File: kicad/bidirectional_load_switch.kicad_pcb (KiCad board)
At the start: 2 copper layers, 10 parts, among them U1 SISS94DN-T1-GE3, U2 RTBS60M, U3 UCC23313DWYR, U4 DMN65D8L-7

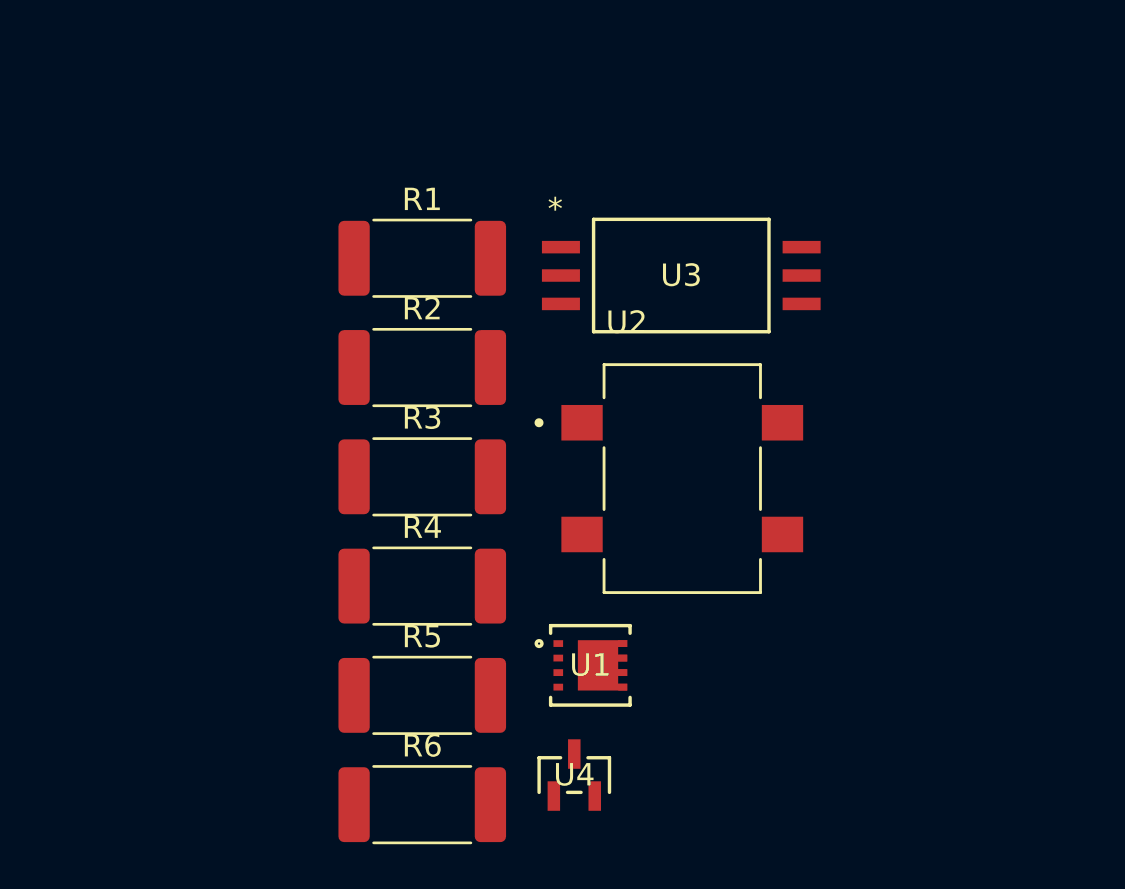
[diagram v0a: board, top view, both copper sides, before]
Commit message: implementing switch design
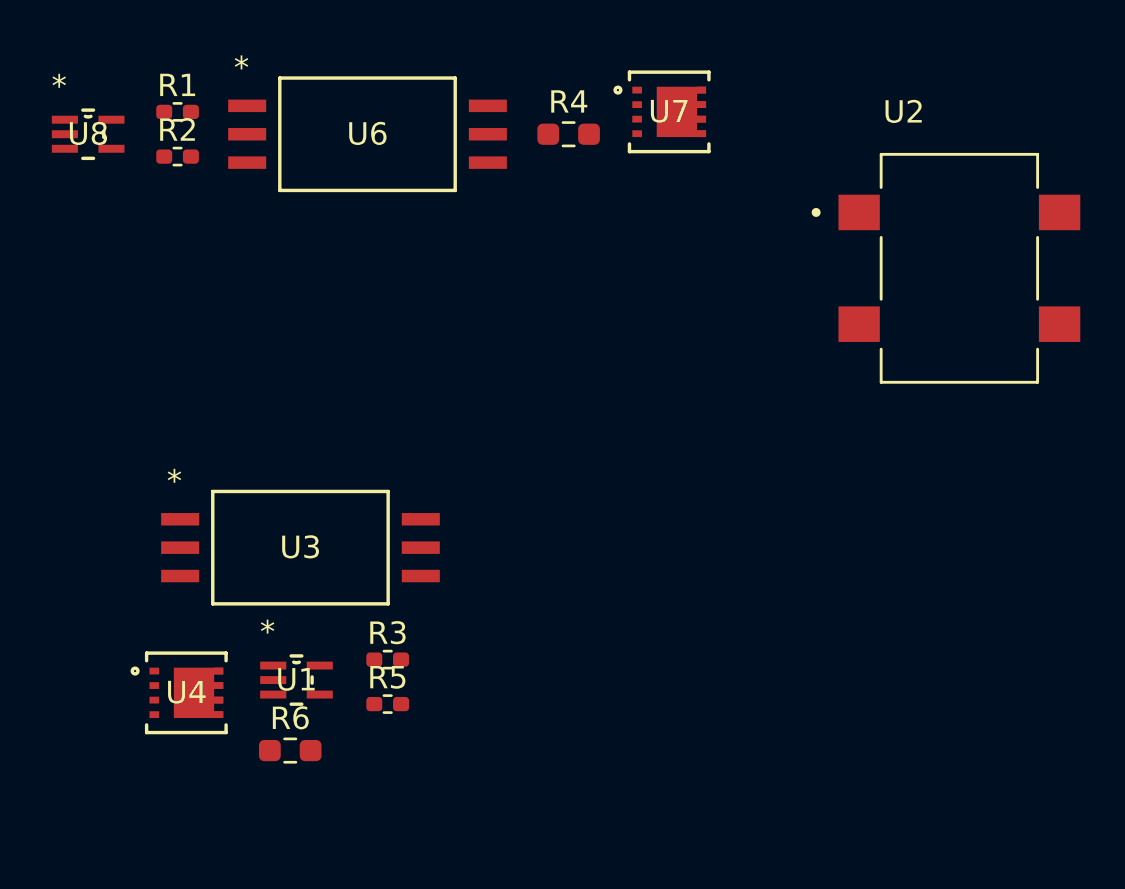
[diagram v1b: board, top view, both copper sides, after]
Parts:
- added U6: UCC23313DWYR, Gate Driver:SOIC6_DWY_TEX, F.Cu at (37.5, 28.0)
- added U7: SISS94DN-T1-GE3, Switching Mosfet:MOSFET_3DN-T1-GE3_VIS, F.Cu at (51.0, 27.0)
- added U8: SN74LVC1G17DCKR, Buffer:DCK5, F.Cu at (25.0, 28.0)
- R1, R2, R3, R5: value R_US -> 50; footprint Resistor_SMD:R_2512_6332Metric_Pad1.40x3.35mm_HandSolder -> Resistor_SMD:R_0402_1005Metric_Pad0.72x0.64mm_HandSolder
- R4, R6: value R_US -> 10; footprint Resistor_SMD:R_2512_6332Metric_Pad1.40x3.35mm_HandSolder -> Resistor_SMD:R_0603_1608Metric_Pad0.98x0.95mm_HandSolder
- U1: value SISS94DN-T1-GE3 -> SN74LVC1G17DCKR; footprint Big Mosfet:MOSFET_3DN-T1-GE3_VIS -> Buffer:DCK5
- U4: value DMN65D8L-7 -> SISS94DN-T1-GE3; footprint Small Mosfet:SOT-23_2P9X1P3_DIO -> Switching Mosfet:MOSFET_3DN-T1-GE3_VIS
- moved R4 21.3 mm to (46.5, 28.0)
- moved U3 20.9 mm to (34.5, 46.5)
- moved U4 17.7 mm to (29.4, 53.0)
- moved U2 15.6 mm to (64.0, 34.0)
- moved R2 14.5 mm to (29.0, 29.0)
- moved U1 13.2 mm to (34.3, 52.4)
- moved R1 12.8 mm to (29.0, 27.0)
- moved R3 8.33 mm to (38.4, 51.5)
- moved R6 6.38 mm to (34.0, 55.6)
- moved R5 1.60 mm to (38.4, 53.5)
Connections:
- R1 pad 1: Net-(U3-VOUT) -> Net-(U8-Y)
- R1 pad 2: Net-(U1-G) -> Net-(U6-ANODE)
- R2 pad 1: GNDPWR -> GND
- R2 pad 2: Net-(U1-G) -> Net-(U6-CATHODE)
- R3 pad 1: Net-(R3-Pad1) -> Net-(U1-Y)
- R3 pad 2: Net-(R3-Pad2) -> Net-(U3-ANODE)
- R4 pad 1: Net-(U3-CATHODE) -> Net-(U6-VOUT)
- R4 pad 2: Net-(U4-D) -> Net-(U7-G)
- R5 pad 1: +3V3 -> GND
- R5 pad 2: Net-(U3-ANODE) -> Net-(U3-CATHODE)
- R6 pad 1: unconnected-(R6-Pad1) -> Net-(U3-VOUT)
- U1 pad 1: GNDPWR -> unconnected-(U1-NC-Pad1)
- U1 pad 2: GNDPWR -> /Switching Channel 1/EN
- U1 pad 3: GNDPWR -> GND
- U1 pad 4: Net-(U1-G) -> Net-(U1-Y)
- U1 pad 5: Net-(R3-Pad2) -> +3V3
- U2 pad 1: Net-(R3-Pad1) -> VS
- U2 pad 3: unconnected-(U2-Pad3) -> Earth
- U2 pad 4: unconnected-(U2-Pad4) -> AC
- U3 pad 6: +15V -> +20V
- U4 pad 1: Net-(U4-G) -> GNDPWR
- U4 pad 2: Net-(U4-D) -> GNDPWR
- U4 pad 3: GNDD -> GNDPWR

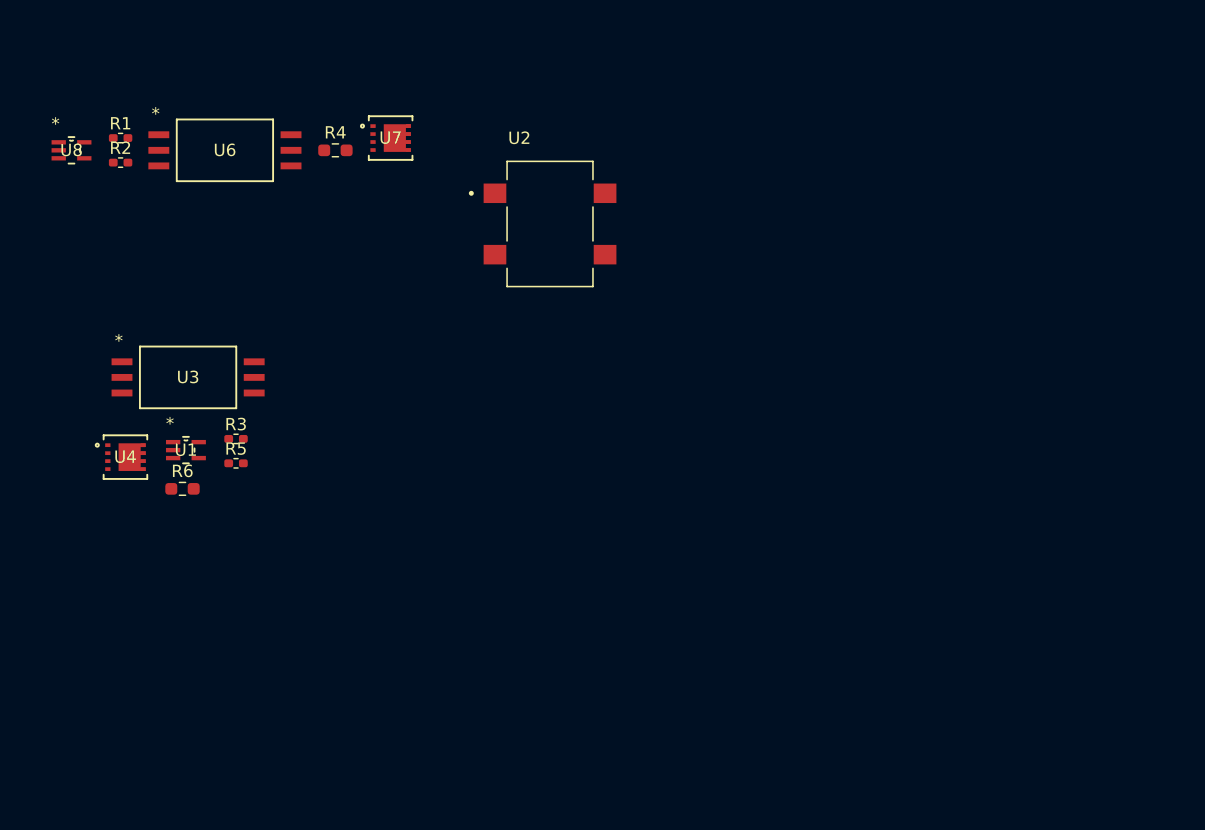
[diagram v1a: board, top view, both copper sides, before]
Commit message: updated switch topology
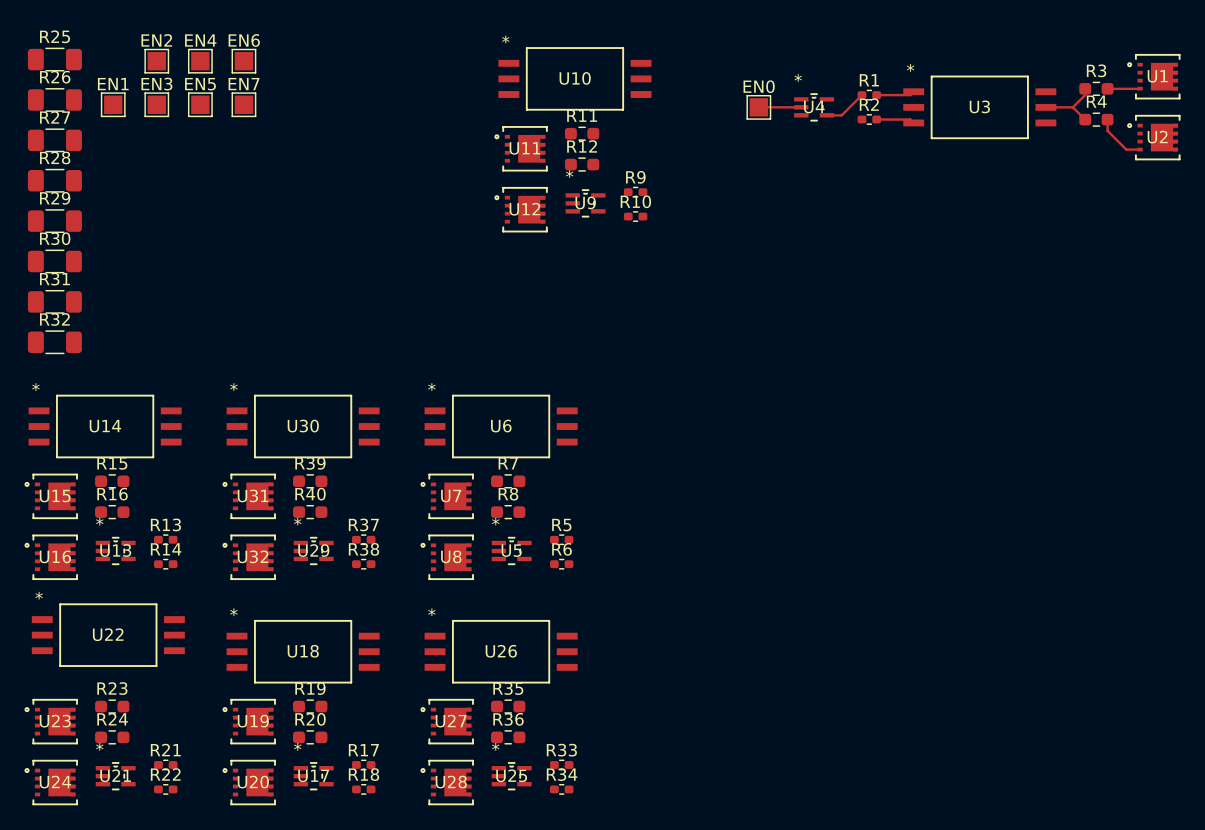
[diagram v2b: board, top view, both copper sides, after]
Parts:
- added EN0: TestPoint, TestPoint:TestPoint_Pad_1.5x1.5mm, F.Cu at (81.0, 24.5)
- added EN1: TestPoint, TestPoint:TestPoint_Pad_1.5x1.5mm, F.Cu at (28.4, 24.3)
- added EN2: TestPoint, TestPoint:TestPoint_Pad_1.5x1.5mm, F.Cu at (31.9, 20.7)
- added EN3: TestPoint, TestPoint:TestPoint_Pad_1.5x1.5mm, F.Cu at (31.9, 24.3)
- added EN4: TestPoint, TestPoint:TestPoint_Pad_1.5x1.5mm, F.Cu at (35.5, 20.7)
- added EN5: TestPoint, TestPoint:TestPoint_Pad_1.5x1.5mm, F.Cu at (35.5, 24.3)
- added EN6: TestPoint, TestPoint:TestPoint_Pad_1.5x1.5mm, F.Cu at (39.0, 20.7)
- added EN7: TestPoint, TestPoint:TestPoint_Pad_1.5x1.5mm, F.Cu at (39.0, 24.3)
- added R10: 50, Resistor_SMD:R_0402_1005Metric_Pad0.72x0.64mm_HandSolder, F.Cu at (71.0, 33.4)
- added R11: 10, Resistor_SMD:R_0603_1608Metric_Pad0.98x0.95mm_HandSolder, F.Cu at (66.6, 26.6)
- added R12: 10, Resistor_SMD:R_0603_1608Metric_Pad0.98x0.95mm_HandSolder, F.Cu at (66.6, 29.2)
- added R13: 50, Resistor_SMD:R_0402_1005Metric_Pad0.72x0.64mm_HandSolder, F.Cu at (32.7, 59.7)
- added R14: 50, Resistor_SMD:R_0402_1005Metric_Pad0.72x0.64mm_HandSolder, F.Cu at (32.7, 61.7)
- added R15: 10, Resistor_SMD:R_0603_1608Metric_Pad0.98x0.95mm_HandSolder, F.Cu at (28.3, 55.0)
- added R16: 10, Resistor_SMD:R_0603_1608Metric_Pad0.98x0.95mm_HandSolder, F.Cu at (28.3, 57.5)
- added R17: 50, Resistor_SMD:R_0402_1005Metric_Pad0.72x0.64mm_HandSolder, F.Cu at (48.8, 78.1)
- added R18: 50, Resistor_SMD:R_0402_1005Metric_Pad0.72x0.64mm_HandSolder, F.Cu at (48.8, 80.1)
- added R19: 10, Resistor_SMD:R_0603_1608Metric_Pad0.98x0.95mm_HandSolder, F.Cu at (44.4, 73.3)
- added R20: 10, Resistor_SMD:R_0603_1608Metric_Pad0.98x0.95mm_HandSolder, F.Cu at (44.4, 75.8)
- added R21: 50, Resistor_SMD:R_0402_1005Metric_Pad0.72x0.64mm_HandSolder, F.Cu at (32.7, 78.1)
- added R22: 50, Resistor_SMD:R_0402_1005Metric_Pad0.72x0.64mm_HandSolder, F.Cu at (32.7, 80.1)
- added R23: 10, Resistor_SMD:R_0603_1608Metric_Pad0.98x0.95mm_HandSolder, F.Cu at (28.3, 73.3)
- added R24: 10, Resistor_SMD:R_0603_1608Metric_Pad0.98x0.95mm_HandSolder, F.Cu at (28.3, 75.8)
- added R25: R_US, Resistor_SMD:R_1206_3216Metric_Pad1.30x1.75mm_HandSolder, F.Cu at (23.6, 20.6)
- added R26: R_US, Resistor_SMD:R_1206_3216Metric_Pad1.30x1.75mm_HandSolder, F.Cu at (23.6, 23.9)
- added R27: R_US, Resistor_SMD:R_1206_3216Metric_Pad1.30x1.75mm_HandSolder, F.Cu at (23.6, 27.2)
- added R28: R_US, Resistor_SMD:R_1206_3216Metric_Pad1.30x1.75mm_HandSolder, F.Cu at (23.6, 30.5)
- added R29: R_US, Resistor_SMD:R_1206_3216Metric_Pad1.30x1.75mm_HandSolder, F.Cu at (23.6, 33.8)
- added R30: R_US, Resistor_SMD:R_1206_3216Metric_Pad1.30x1.75mm_HandSolder, F.Cu at (23.6, 37.1)
- added R31: R_US, Resistor_SMD:R_1206_3216Metric_Pad1.30x1.75mm_HandSolder, F.Cu at (23.6, 40.3)
- added R32: R_US, Resistor_SMD:R_1206_3216Metric_Pad1.30x1.75mm_HandSolder, F.Cu at (23.6, 43.6)
- added R33: 50, Resistor_SMD:R_0402_1005Metric_Pad0.72x0.64mm_HandSolder, F.Cu at (64.9, 78.1)
- added R34: 50, Resistor_SMD:R_0402_1005Metric_Pad0.72x0.64mm_HandSolder, F.Cu at (64.9, 80.1)
- added R35: 10, Resistor_SMD:R_0603_1608Metric_Pad0.98x0.95mm_HandSolder, F.Cu at (60.6, 73.3)
- added R36: 10, Resistor_SMD:R_0603_1608Metric_Pad0.98x0.95mm_HandSolder, F.Cu at (60.6, 75.8)
- added R37: 50, Resistor_SMD:R_0402_1005Metric_Pad0.72x0.64mm_HandSolder, F.Cu at (48.8, 59.7)
- added R38: 50, Resistor_SMD:R_0402_1005Metric_Pad0.72x0.64mm_HandSolder, F.Cu at (48.8, 61.7)
- added R39: 10, Resistor_SMD:R_0603_1608Metric_Pad0.98x0.95mm_HandSolder, F.Cu at (44.4, 55.0)
- added R40: 10, Resistor_SMD:R_0603_1608Metric_Pad0.98x0.95mm_HandSolder, F.Cu at (44.4, 57.5)
- added R7: 10, Resistor_SMD:R_0603_1608Metric_Pad0.98x0.95mm_HandSolder, F.Cu at (60.6, 55.0)
- added R8: 10, Resistor_SMD:R_0603_1608Metric_Pad0.98x0.95mm_HandSolder, F.Cu at (60.6, 57.5)
- added R9: 50, Resistor_SMD:R_0402_1005Metric_Pad0.72x0.64mm_HandSolder, F.Cu at (71.0, 31.4)
- added U10: UCC23313DWYR, Gate Driver:SOIC6_DWY_TEX, F.Cu at (66.0, 22.2)
- added U11: SISS94DN-T1-GE3, Switching Mosfet:MOSFET_3DN-T1-GE3_VIS, F.Cu at (62.0, 27.9)
- added U12: SISS94DN-T1-GE3, Switching Mosfet:MOSFET_3DN-T1-GE3_VIS, F.Cu at (62.0, 32.8)
- added U13: SN74LVC1G17DCKR, Buffer:DCK5, F.Cu at (28.6, 60.6)
- added U14: UCC23313DWYR, Gate Driver:SOIC6_DWY_TEX, F.Cu at (27.7, 50.5)
- added U15: SISS94DN-T1-GE3, Switching Mosfet:MOSFET_3DN-T1-GE3_VIS, F.Cu at (23.7, 56.2)
- added U16: SISS94DN-T1-GE3, Switching Mosfet:MOSFET_3DN-T1-GE3_VIS, F.Cu at (23.7, 61.2)
- added U17: SN74LVC1G17DCKR, Buffer:DCK5, F.Cu at (44.7, 79.0)
- added U18: UCC23313DWYR, Gate Driver:SOIC6_DWY_TEX, F.Cu at (43.9, 68.8)
- added U19: SISS94DN-T1-GE3, Switching Mosfet:MOSFET_3DN-T1-GE3_VIS, F.Cu at (39.8, 74.5)
- added U20: SISS94DN-T1-GE3, Switching Mosfet:MOSFET_3DN-T1-GE3_VIS, F.Cu at (39.8, 79.5)
- added U21: SN74LVC1G17DCKR, Buffer:DCK5, F.Cu at (28.6, 79.0)
- added U22: UCC23313DWYR, Gate Driver:SOIC6_DWY_TEX, F.Cu at (28.0, 67.5)
- added U23: SISS94DN-T1-GE3, Switching Mosfet:MOSFET_3DN-T1-GE3_VIS, F.Cu at (23.7, 74.5)
- added U24: SISS94DN-T1-GE3, Switching Mosfet:MOSFET_3DN-T1-GE3_VIS, F.Cu at (23.7, 79.5)
- added U25: SN74LVC1G17DCKR, Buffer:DCK5, F.Cu at (60.9, 79.0)
- added U26: UCC23313DWYR, Gate Driver:SOIC6_DWY_TEX, F.Cu at (60.0, 68.8)
- added U27: SISS94DN-T1-GE3, Switching Mosfet:MOSFET_3DN-T1-GE3_VIS, F.Cu at (55.9, 74.5)
- added U28: SISS94DN-T1-GE3, Switching Mosfet:MOSFET_3DN-T1-GE3_VIS, F.Cu at (55.9, 79.5)
- added U29: SN74LVC1G17DCKR, Buffer:DCK5, F.Cu at (44.7, 60.6)
- added U30: UCC23313DWYR, Gate Driver:SOIC6_DWY_TEX, F.Cu at (43.9, 50.5)
- added U31: SISS94DN-T1-GE3, Switching Mosfet:MOSFET_3DN-T1-GE3_VIS, F.Cu at (39.8, 56.2)
- added U32: SISS94DN-T1-GE3, Switching Mosfet:MOSFET_3DN-T1-GE3_VIS, F.Cu at (39.8, 61.2)
- added U5: SN74LVC1G17DCKR, Buffer:DCK5, F.Cu at (60.9, 60.6)
- added U9: SN74LVC1G17DCKR, Buffer:DCK5, F.Cu at (66.9, 32.3)
- R3: value 50 -> 10; footprint Resistor_SMD:R_0402_1005Metric_Pad0.72x0.64mm_HandSolder -> Resistor_SMD:R_0603_1608Metric_Pad0.98x0.95mm_HandSolder
- R6: value 10 -> 50; footprint Resistor_SMD:R_0603_1608Metric_Pad0.98x0.95mm_HandSolder -> Resistor_SMD:R_0402_1005Metric_Pad0.72x0.64mm_HandSolder
- U1, U8: value SN74LVC1G17DCKR -> SISS94DN-T1-GE3; footprint Buffer:DCK5 -> Switching Mosfet:MOSFET_3DN-T1-GE3_VIS
- U2: value RTBS60M -> SISS94DN-T1-GE3; footprint Rectifier:SOIC500P990X195-4N -> Switching Mosfet:MOSFET_3DN-T1-GE3_VIS
- U4: value SISS94DN-T1-GE3 -> SN74LVC1G17DCKR; footprint Switching Mosfet:MOSFET_3DN-T1-GE3_VIS -> Buffer:DCK5
- moved U1 84.8 mm to (113.5, 22.0)
- moved R3 75.7 mm to (108.5, 23.0)
- moved U3 68.1 mm to (99.0, 24.5)
- moved U4 62.9 mm to (85.5, 24.5)
- moved R4 62.1 mm to (108.5, 25.5)
- moved R2 61.1 mm to (90.0, 25.5)
- moved R1 61.1 mm to (90.0, 23.5)
- moved U2 50.0 mm to (113.5, 27.0)
- moved U8 45.3 mm to (55.9, 61.2)
- moved U6 31.8 mm to (60.0, 50.5)
- moved R6 31.5 mm to (64.9, 61.7)
- moved U7 29.6 mm to (55.9, 56.2)
- moved R5 27.3 mm to (64.9, 59.7)
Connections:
- net /Switching Channel 0/IN renamed /Channel 1/IN
- R1 pad 1: Net-(U8-Y) -> Net-(U4-Y)
- R1 pad 2: Net-(U6-ANODE) -> Net-(U3-ANODE)
- R2 pad 2: Net-(U6-CATHODE) -> Net-(U3-CATHODE)
- R3 pad 1: Net-(U1-Y) -> Net-(U3-VOUT)
- R3 pad 2: Net-(U3-ANODE) -> Net-(U1-G)
- R4 pad 1: Net-(U6-VOUT) -> Net-(U3-VOUT)
- R4 pad 2: Net-(U7-G) -> Net-(U2-G)
- R5 pad 1: GND -> Net-(U5-Y)
- R5 pad 2: Net-(U3-CATHODE) -> Net-(U6-ANODE)
- R6 pad 1: Net-(U3-VOUT) -> GND
- R6 pad 2: Net-(U4-G) -> Net-(U6-CATHODE)
- U1 pad 1: unconnected-(U1-NC-Pad1) -> GNDPWR
- U1 pad 2: /Switching Channel 1/EN -> GNDPWR
- U1 pad 3: GND -> GNDPWR
- U1 pad 4: Net-(U1-Y) -> Net-(U1-G)
- U1 pad 5: +3V3 -> /Channel 0/IN
- U2 pad 1: VS -> GNDPWR
- U2 pad 3: Earth -> GNDPWR
- U2 pad 4: AC -> Net-(U2-G)
- U4 pad 1: GNDPWR -> unconnected-(U4-NC-Pad1)
- U4 pad 2: GNDPWR -> /Channel 0/EN
- U4 pad 3: GNDPWR -> GND
- U4 pad 4: Net-(U4-G) -> Net-(U4-Y)
- U4 pad 5: /Switching Channel 1/IN -> +3V3
- U8 pad 1: unconnected-(U8-NC-Pad1) -> GNDPWR
- U8 pad 2: /Switching Channel 0/EN -> GNDPWR
- U8 pad 3: GND -> GNDPWR
- U8 pad 4: Net-(U8-Y) -> Net-(U8-G)
- U8 pad 5: +3V3 -> Earth
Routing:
- net Net-(U3-VOUT): track 0.00 -> 5.54 mm
- net Net-(U2-G): track 0.00 -> 4.20 mm
- net Net-(U4-Y): track 0.00 -> 3.54 mm
- net /Channel 0/EN: track 0.00 -> 3.46 mm
- net Net-(U3-CATHODE): track 0.00 -> 3.13 mm
- net Net-(U3-ANODE): track 0.00 -> 3.13 mm
- net Net-(U1-G): track 0.00 -> 2.66 mm

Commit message: kicad
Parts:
- removed EN0, EN1, EN2, EN3, EN4, EN5, EN6, EN7: TestPoint, TestPoint:TestPoint_Pad_1.5x1.5mm
- removed R1, R10, R13, R14, R17, R18, R2, R21, R22, R33, R34, R37, R38, R5, R6, R9: 50, Resistor_SMD:R_0402_1005Metric_Pad0.72x0.64mm_HandSolder
- removed R11, R12, R15, R16, R19, R20, R23, R24, R3, R35, R36, R39, R4, R40, R7, R8: 10, Resistor_SMD:R_0603_1608Metric_Pad0.98x0.95mm_HandSolder
- removed R25, R26, R27, R28, R29, R30, R31, R32: R_US, Resistor_SMD:R_1206_3216Metric_Pad1.30x1.75mm_HandSolder
- removed U1, U11, U12, U15, U16, U19, U2, U20, U23, U24, U27, U28, U31, U32, U7, U8: SISS94DN-T1-GE3, Switching Mosfet:MOSFET_3DN-T1-GE3_VIS
- removed U10, U14, U18, U22, U26, U3, U30, U6: UCC23313DWYR, Gate Driver:SOIC6_DWY_TEX
- removed U13, U17, U21, U25, U29, U4, U5, U9: SN74LVC1G17DCKR, Buffer:DCK5
- added C1001: 10u, Capacitor_SMD:C_1206_3216Metric, F.Cu at (31.5, 68.5)
- added C1002: 10u, Capacitor_SMD:C_1206_3216Metric, F.Cu at (31.5, 71.8)
- added C1003: 100n, Capacitor_SMD:C_0402_1005Metric, F.Cu at (50.7, 81.9)
- added C1004: 10u, Capacitor_SMD:C_1206_3216Metric, F.Cu at (31.5, 75.2)
- added C1005: 10u, Capacitor_SMD:C_1206_3216Metric, F.Cu at (31.5, 78.5)
- added C1006: 10u, Capacitor_SMD:C_1206_3216Metric, F.Cu at (31.5, 81.9)
- added C1007: 10u, Capacitor_SMD:C_1206_3216Metric, F.Cu at (31.5, 85.2)
- added C1008: 100n, Capacitor_SMD:C_0402_1005Metric, F.Cu at (50.7, 83.9)
- added C201: 1u, Capacitor_SMD:C_0402_1005Metric, F.Cu at (81.9, 30.9)
- added C202: 100n, Capacitor_SMD:C_0402_1005Metric, F.Cu at (81.9, 32.9)
- added C203: 10u, Capacitor_SMD:C_1206_3216Metric, F.Cu at (69.1, 38.0)
- added C204: 100n, Capacitor_SMD:C_0402_1005Metric, F.Cu at (81.9, 34.8)
- added C301: 1u, Capacitor_SMD:C_0402_1005Metric, F.Cu at (100.9, 85.9)
- added C302: 100n, Capacitor_SMD:C_0402_1005Metric, F.Cu at (100.9, 87.9)
- added C303: 10u, Capacitor_SMD:C_1206_3216Metric, F.Cu at (88.1, 93.1)
- added C304: 100n, Capacitor_SMD:C_0402_1005Metric, F.Cu at (100.9, 89.9)
- added C401: 1u, Capacitor_SMD:C_0402_1005Metric, F.Cu at (100.9, 67.6)
- added C402: 100n, Capacitor_SMD:C_0402_1005Metric, F.Cu at (100.9, 69.6)
- added C403: 10u, Capacitor_SMD:C_1206_3216Metric, F.Cu at (88.1, 74.7)
- added C404: 100n, Capacitor_SMD:C_0402_1005Metric, F.Cu at (100.9, 71.5)
- added C501: 1u, Capacitor_SMD:C_0402_1005Metric, F.Cu at (100.9, 49.2)
- added C502: 100n, Capacitor_SMD:C_0402_1005Metric, F.Cu at (100.9, 51.2)
- added C503: 10u, Capacitor_SMD:C_1206_3216Metric, F.Cu at (88.1, 56.4)
- added C504: 100n, Capacitor_SMD:C_0402_1005Metric, F.Cu at (100.9, 53.2)
- added C601: 1u, Capacitor_SMD:C_0402_1005Metric, F.Cu at (81.9, 67.6)
- added C602: 100n, Capacitor_SMD:C_0402_1005Metric, F.Cu at (81.9, 69.6)
- added C603: 10u, Capacitor_SMD:C_1206_3216Metric, F.Cu at (69.1, 74.7)
- added C604: 100n, Capacitor_SMD:C_0402_1005Metric, F.Cu at (81.9, 71.5)
- added C701: 1u, Capacitor_SMD:C_0402_1005Metric, F.Cu at (81.9, 85.9)
- added C702: 100n, Capacitor_SMD:C_0402_1005Metric, F.Cu at (81.9, 87.9)
- added C703: 10u, Capacitor_SMD:C_1206_3216Metric, F.Cu at (69.1, 93.1)
- added C704: 100n, Capacitor_SMD:C_0402_1005Metric, F.Cu at (81.9, 89.9)
- added C801: 1u, Capacitor_SMD:C_0402_1005Metric, F.Cu at (100.9, 30.9)
- added C802: 100n, Capacitor_SMD:C_0402_1005Metric, F.Cu at (100.9, 32.9)
- added C803: 10u, Capacitor_SMD:C_1206_3216Metric, F.Cu at (88.1, 38.0)
- added C804: 100n, Capacitor_SMD:C_0402_1005Metric, F.Cu at (100.9, 34.8)
- added C901: 1u, Capacitor_SMD:C_0402_1005Metric, F.Cu at (81.9, 49.2)
- added C902: 100n, Capacitor_SMD:C_0402_1005Metric, F.Cu at (81.9, 51.2)
- added C903: 10u, Capacitor_SMD:C_1206_3216Metric, F.Cu at (69.1, 56.4)
- added C904: 100n, Capacitor_SMD:C_0402_1005Metric, F.Cu at (81.9, 53.2)
- added C_{SNB}1001: 22p, Capacitor_SMD:C_0402_1005Metric, F.Cu at (50.7, 85.9)
- added Css1001: 100n, Capacitor_SMD:C_0402_1005Metric, F.Cu at (50.7, 87.8)
- added D_{C}1001: PDZVTR9.1B, zener_PDZVTR9.1B:DIO_PDZVTFT_ROM, F.Cu at (45.8, 83.0)
- added D_{FLY}1001: SK510A-LTP, schottky_SK510A-LTP:SMADO-214AC_LEAD-FRAME_MCC, F.Cu at (38.3, 83.2)
- added D_{F}1001: SK510A-LTP, schottky_SK510A-LTP:SMADO-214AC_LEAD-FRAME_MCC, F.Cu at (38.3, 87.8)
- added D_{Z}1001: PDZVTR9.1B, zener_PDZVTR9.1B:DIO_PDZVTFT_ROM, F.Cu at (45.8, 87.2)
- added J101: Screw_Terminal_01x13, TerminalBlock:TerminalBlock_Xinya_XY308-2.54-13P_1x13_P2.54mm_Horizontal, F.Cu at (31.3, 34.0)
- added R201: 50, Resistor_SMD:R_0402_1005Metric_Pad0.72x0.64mm_HandSolder, F.Cu at (67.9, 40.7)
- added R202: 50, Resistor_SMD:R_0402_1005Metric_Pad0.72x0.64mm_HandSolder, F.Cu at (67.9, 42.7)
- added R203: 5, Resistor_SMD:R_0603_1608Metric_Pad0.98x0.95mm_HandSolder, F.Cu at (79.6, 41.4)
- added R204: 5, Resistor_SMD:R_0603_1608Metric_Pad0.98x0.95mm_HandSolder, F.Cu at (79.6, 43.9)
- added R301: 50, Resistor_SMD:R_0402_1005Metric_Pad0.72x0.64mm_HandSolder, F.Cu at (86.9, 95.7)
- added R302: 50, Resistor_SMD:R_0402_1005Metric_Pad0.72x0.64mm_HandSolder, F.Cu at (86.9, 97.7)
- added R303: 5, Resistor_SMD:R_0603_1608Metric_Pad0.98x0.95mm_HandSolder, F.Cu at (98.6, 96.5)
- added R304: 5, Resistor_SMD:R_0603_1608Metric_Pad0.98x0.95mm_HandSolder, F.Cu at (98.6, 99.0)
- added R401: 50, Resistor_SMD:R_0402_1005Metric_Pad0.72x0.64mm_HandSolder, F.Cu at (86.9, 77.4)
- added R402: 50, Resistor_SMD:R_0402_1005Metric_Pad0.72x0.64mm_HandSolder, F.Cu at (86.9, 79.4)
- added R403: 5, Resistor_SMD:R_0603_1608Metric_Pad0.98x0.95mm_HandSolder, F.Cu at (98.6, 78.1)
- added R404: 5, Resistor_SMD:R_0603_1608Metric_Pad0.98x0.95mm_HandSolder, F.Cu at (98.6, 80.6)
- added R501: 50, Resistor_SMD:R_0402_1005Metric_Pad0.72x0.64mm_HandSolder, F.Cu at (86.9, 59.0)
- added R502: 50, Resistor_SMD:R_0402_1005Metric_Pad0.72x0.64mm_HandSolder, F.Cu at (86.9, 61.0)
- added R503: 5, Resistor_SMD:R_0603_1608Metric_Pad0.98x0.95mm_HandSolder, F.Cu at (98.6, 59.8)
- added R504: 5, Resistor_SMD:R_0603_1608Metric_Pad0.98x0.95mm_HandSolder, F.Cu at (98.6, 62.3)
- added R601: 50, Resistor_SMD:R_0402_1005Metric_Pad0.72x0.64mm_HandSolder, F.Cu at (67.9, 77.4)
- added R602: 50, Resistor_SMD:R_0402_1005Metric_Pad0.72x0.64mm_HandSolder, F.Cu at (67.9, 79.4)
- added R603: 5, Resistor_SMD:R_0603_1608Metric_Pad0.98x0.95mm_HandSolder, F.Cu at (79.6, 78.1)
- added R604: 5, Resistor_SMD:R_0603_1608Metric_Pad0.98x0.95mm_HandSolder, F.Cu at (79.6, 80.6)
- added R701: 50, Resistor_SMD:R_0402_1005Metric_Pad0.72x0.64mm_HandSolder, F.Cu at (67.9, 95.7)
- added R702: 50, Resistor_SMD:R_0402_1005Metric_Pad0.72x0.64mm_HandSolder, F.Cu at (67.9, 97.7)
- added R703: 5, Resistor_SMD:R_0603_1608Metric_Pad0.98x0.95mm_HandSolder, F.Cu at (79.6, 96.5)
- added R704: 5, Resistor_SMD:R_0603_1608Metric_Pad0.98x0.95mm_HandSolder, F.Cu at (79.6, 99.0)
- added R801: 50, Resistor_SMD:R_0402_1005Metric_Pad0.72x0.64mm_HandSolder, F.Cu at (86.9, 40.7)
- added R802: 50, Resistor_SMD:R_0402_1005Metric_Pad0.72x0.64mm_HandSolder, F.Cu at (86.9, 42.7)
- added R803: 5, Resistor_SMD:R_0603_1608Metric_Pad0.98x0.95mm_HandSolder, F.Cu at (98.6, 41.4)
- added R804: 5, Resistor_SMD:R_0603_1608Metric_Pad0.98x0.95mm_HandSolder, F.Cu at (98.6, 43.9)
- added R901: 50, Resistor_SMD:R_0402_1005Metric_Pad0.72x0.64mm_HandSolder, F.Cu at (67.9, 59.0)
- added R902: 50, Resistor_SMD:R_0402_1005Metric_Pad0.72x0.64mm_HandSolder, F.Cu at (67.9, 61.0)
- added R903: 5, Resistor_SMD:R_0603_1608Metric_Pad0.98x0.95mm_HandSolder, F.Cu at (79.6, 59.8)
- added R904: 5, Resistor_SMD:R_0603_1608Metric_Pad0.98x0.95mm_HandSolder, F.Cu at (79.6, 62.3)
- added RS101: R_US, Resistor_SMD:R_1206_3216Metric_Pad1.30x1.75mm_HandSolder, F.Cu at (31.7, 40.1)
- added RS102: R_US, Resistor_SMD:R_1206_3216Metric_Pad1.30x1.75mm_HandSolder, F.Cu at (31.7, 43.4)
- added RS103: R_US, Resistor_SMD:R_1206_3216Metric_Pad1.30x1.75mm_HandSolder, F.Cu at (31.7, 46.7)
- added RS104: R_US, Resistor_SMD:R_1206_3216Metric_Pad1.30x1.75mm_HandSolder, F.Cu at (31.7, 50.0)
- added RS105: R_US, Resistor_SMD:R_1206_3216Metric_Pad1.30x1.75mm_HandSolder, F.Cu at (31.7, 53.3)
- added RS106: R_US, Resistor_SMD:R_1206_3216Metric_Pad1.30x1.75mm_HandSolder, F.Cu at (31.7, 56.6)
- added RS107: R_US, Resistor_SMD:R_1206_3216Metric_Pad1.30x1.75mm_HandSolder, F.Cu at (31.7, 59.8)
- added RS108: R_US, Resistor_SMD:R_1206_3216Metric_Pad1.30x1.75mm_HandSolder, F.Cu at (31.7, 63.1)
- added R_{DUMMY}1001: 1.5k, Resistor_SMD:R_0402_1005Metric, F.Cu at (53.4, 67.8)
- added R_{FB}1001: 196k, Resistor_SMD:R_0402_1005Metric, F.Cu at (53.4, 69.8)
- added R_{SET}1001: 12.1k, Resistor_SMD:R_0402_1005Metric, F.Cu at (53.4, 71.8)
- added R_{SNB}1001: 100, Resistor_SMD:R_0402_1005Metric, F.Cu at (53.4, 73.7)
- added Rtc1001: 787k, Resistor_SMD:R_0402_1005Metric, F.Cu at (53.4, 75.7)
- added Ruv1001: 46.4k, Resistor_SMD:R_0402_1005Metric, F.Cu at (53.4, 77.7)
- added Ruv1002: 10.7k, Resistor_SMD:R_0402_1005Metric, F.Cu at (53.4, 79.7)
- added U1001: LM25184NGUR, dc_to_dc_LM25184NGUR:NGU0008C-IPC_A, F.Cu at (53.0, 91.4)
- added U1002: 750313445, transformer_750313445:SOIC_13445_WRE, F.Cu at (43.2, 73.9)
- added U201: SN74LVC1G17DCKR, buffer_SN74LVC1G17DCKR:DCK5, F.Cu at (79.9, 38.3)
- added U202: UCC23313DWYR, gate_driver_UCC23313DWYR:SOIC6_DWY_TEX, F.Cu at (73.4, 33.1)
- added U203: SISS94DN-T1-GE3, mosfet_SISS94DN-T1-GE3:MOSFET_3DN-T1-GE3_VIS, F.Cu at (74.9, 38.8)
- added U204: SISS94DN-T1-GE3, mosfet_SISS94DN-T1-GE3:MOSFET_3DN-T1-GE3_VIS, F.Cu at (74.9, 43.8)
- added U301: SN74LVC1G17DCKR, buffer_SN74LVC1G17DCKR:DCK5, F.Cu at (98.9, 93.3)
- added U302: UCC23313DWYR, gate_driver_UCC23313DWYR:SOIC6_DWY_TEX, F.Cu at (92.4, 88.2)
- added U303: SISS94DN-T1-GE3, mosfet_SISS94DN-T1-GE3:MOSFET_3DN-T1-GE3_VIS, F.Cu at (93.9, 93.9)
- added U304: SISS94DN-T1-GE3, mosfet_SISS94DN-T1-GE3:MOSFET_3DN-T1-GE3_VIS, F.Cu at (93.9, 98.8)
- added U401: SN74LVC1G17DCKR, buffer_SN74LVC1G17DCKR:DCK5, F.Cu at (98.9, 75.0)
- added U402: UCC23313DWYR, gate_driver_UCC23313DWYR:SOIC6_DWY_TEX, F.Cu at (92.4, 69.8)
- added U403: SISS94DN-T1-GE3, mosfet_SISS94DN-T1-GE3:MOSFET_3DN-T1-GE3_VIS, F.Cu at (93.9, 75.5)
- added U404: SISS94DN-T1-GE3, mosfet_SISS94DN-T1-GE3:MOSFET_3DN-T1-GE3_VIS, F.Cu at (93.9, 80.5)
- added U501: SN74LVC1G17DCKR, buffer_SN74LVC1G17DCKR:DCK5, F.Cu at (98.9, 56.6)
- added U502: UCC23313DWYR, gate_driver_UCC23313DWYR:SOIC6_DWY_TEX, F.Cu at (92.4, 51.5)
- added U503: SISS94DN-T1-GE3, mosfet_SISS94DN-T1-GE3:MOSFET_3DN-T1-GE3_VIS, F.Cu at (93.9, 57.2)
- added U504: SISS94DN-T1-GE3, mosfet_SISS94DN-T1-GE3:MOSFET_3DN-T1-GE3_VIS, F.Cu at (93.9, 62.1)
- added U601: SN74LVC1G17DCKR, buffer_SN74LVC1G17DCKR:DCK5, F.Cu at (79.9, 75.0)
- added U602: UCC23313DWYR, gate_driver_UCC23313DWYR:SOIC6_DWY_TEX, F.Cu at (73.4, 69.8)
- added U603: SISS94DN-T1-GE3, mosfet_SISS94DN-T1-GE3:MOSFET_3DN-T1-GE3_VIS, F.Cu at (74.9, 75.5)
- added U604: SISS94DN-T1-GE3, mosfet_SISS94DN-T1-GE3:MOSFET_3DN-T1-GE3_VIS, F.Cu at (74.9, 80.5)
- added U701: SN74LVC1G17DCKR, buffer_SN74LVC1G17DCKR:DCK5, F.Cu at (79.9, 93.3)
- added U702: UCC23313DWYR, gate_driver_UCC23313DWYR:SOIC6_DWY_TEX, F.Cu at (73.4, 88.2)
- added U703: SISS94DN-T1-GE3, mosfet_SISS94DN-T1-GE3:MOSFET_3DN-T1-GE3_VIS, F.Cu at (74.9, 93.9)
- added U704: SISS94DN-T1-GE3, mosfet_SISS94DN-T1-GE3:MOSFET_3DN-T1-GE3_VIS, F.Cu at (74.9, 98.8)
- added U801: SN74LVC1G17DCKR, buffer_SN74LVC1G17DCKR:DCK5, F.Cu at (98.9, 38.3)
- added U802: UCC23313DWYR, gate_driver_UCC23313DWYR:SOIC6_DWY_TEX, F.Cu at (92.4, 33.1)
- added U803: SISS94DN-T1-GE3, mosfet_SISS94DN-T1-GE3:MOSFET_3DN-T1-GE3_VIS, F.Cu at (93.9, 38.8)
- added U804: SISS94DN-T1-GE3, mosfet_SISS94DN-T1-GE3:MOSFET_3DN-T1-GE3_VIS, F.Cu at (93.9, 43.8)
- added U901: SN74LVC1G17DCKR, buffer_SN74LVC1G17DCKR:DCK5, F.Cu at (79.9, 56.6)
- added U902: UCC23313DWYR, gate_driver_UCC23313DWYR:SOIC6_DWY_TEX, F.Cu at (73.4, 51.5)
- added U903: SISS94DN-T1-GE3, mosfet_SISS94DN-T1-GE3:MOSFET_3DN-T1-GE3_VIS, F.Cu at (74.9, 57.2)
- added U904: SISS94DN-T1-GE3, mosfet_SISS94DN-T1-GE3:MOSFET_3DN-T1-GE3_VIS, F.Cu at (74.9, 62.1)
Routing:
- net Net-(U3-VOUT): track 5.54 -> 0.00 mm
- net Net-(U2-G): track 4.20 -> 0.00 mm
- net Net-(U4-Y): track 3.54 -> 0.00 mm
- net /Channel 0/EN: track 3.46 -> 0.00 mm
- net Net-(U3-CATHODE): track 3.13 -> 0.00 mm
- net Net-(U3-ANODE): track 3.13 -> 0.00 mm
- net Net-(U1-G): track 2.66 -> 0.00 mm
